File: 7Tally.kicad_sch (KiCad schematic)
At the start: 24 parts, among them J2 B2B-PH-K-S_LF__SN_, P1 53047-0310, SW1 TL3300CF160Q, U1 ESP32-C3_SUPERMINI_TH, U2 BQ21040DBVR, U3 TC1263-3.3VOA

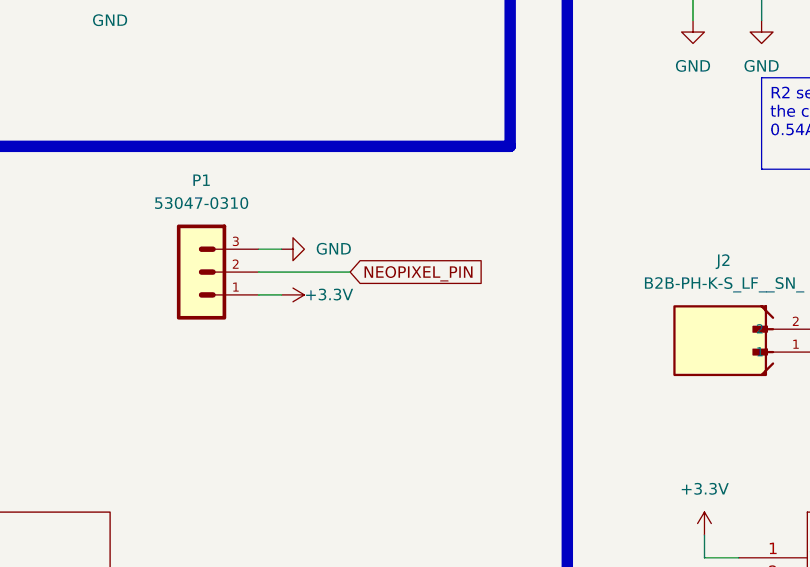
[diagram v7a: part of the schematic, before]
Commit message: feat(PCB): finalized initial PCB
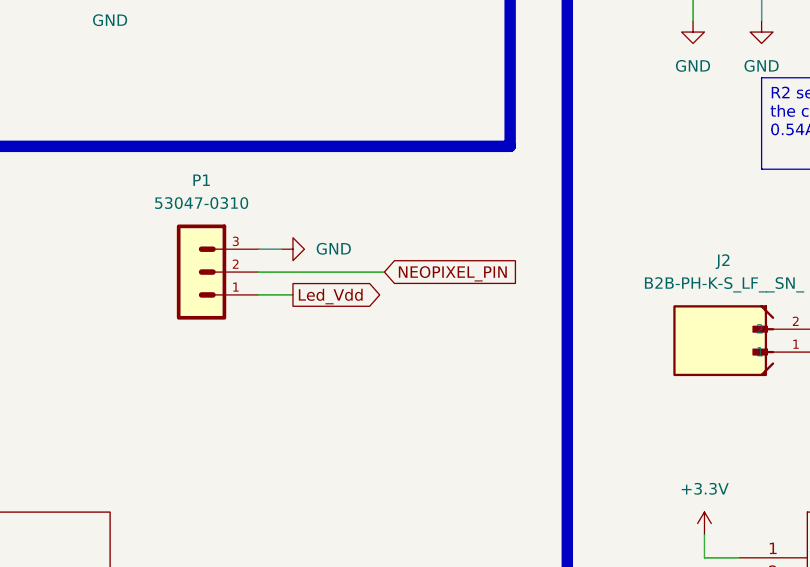
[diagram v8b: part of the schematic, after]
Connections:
- net +3.3V: no longer P1.1
- net Led_Vdd: now also P1.1
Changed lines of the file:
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@@
 	(wire
 		(pts
-			(xy 93.98 95.25) (xy 104.14 95.25)
+			(xy 93.98 95.25) (xy 107.95 95.25)
 		)
 		(stroke
@@
 	(wire
 		(pts
-			(xy 96.52 97.79) (xy 93.98 97.79)
+			(xy 97.79 97.79) (xy 93.98 97.79)
 		)
 		(stroke
@@
 	(global_label "NEOPIXEL_PIN"
 		(shape input)
-		(at 104.14 95.25 0)
+		(at 107.95 95.25 0)
 		(fields_autoplaced yes)
 		(effects
@@
 		)
 		(property "Intersheetrefs" "${INTERSHEET_REFS}"
-			(at 120.3695 95.25 0)
+			(at 124.1795 95.25 0)
 			(effects
 				(font
@@
 				)
 				(justify right)
+				(hide yes)
+			)
+		)
+	)
+	(global_label "Led_Vdd"
+		(shape output)
+		(at 97.79 97.79 0)
+		(fields_autoplaced yes)
+		(effects
+			(font
+				(size 1.27 1.27)
+			)
+			(justify left)
+		)
+		(property "Intersheetrefs" "${INTERSHEET_REFS}"
+			(at 108.3951 97.79 0)
+			(effects
+				(font
+					(size 1.27 1.27)
+				)
+				(justify left)
 				(hide yes)
 			)
@@
 					(unit 1)
 				)
-			)
-		)
-	)
-	(symbol
-		(lib_id "power:+3.3V")
-		(at 96.52 97.79 270)
-		(unit 1)
-		(exclude_from_sim no)
-		(in_bom yes)
-		(on_board yes)
-		(dnp no)
-		(property "Reference" "#PWR022"
-			(at 92.71 97.79 0)
-			(effects
-				(font
-					(size 1.27 1.27)
-				)
-				(hide yes)
-			)
-		)
-		(property "Value" "+3.3V"
-			(at 99.06 97.79 90)
-			(effects
-				(font
-					(size 1.27 1.27)
-				)
-				(justify left)
-			)
-		)
-		(property "Footprint" ""
-			(at 96.52 97.79 0)
-			(effects
-				(font
-					(size 1.27 1.27)
-				)
-				(hide yes)
-			)
-		)
-		(property "Datasheet" ""
-			(at 96.52 97.79 0)
-			(effects
-				(font
-					(size 1.27 1.27)
-				)
-				(hide yes)
-			)
-		)
-		(property "Description" "Power symbol creates a global label with name \"+3.3V\""
-			(at 96.52 97.79 0)
-			(effects
-				(font
-					(size 1.27 1.27)
-				)
-				(hide yes)
-			)
-		)
-		(pin "1"
-		)
-		(instances
-			(project "7Tally"
-				(path "/a26cb5f3-8ba9-4d03-a29e-a58d33583019"
-					(reference "#PWR022")
-					(unit 1)
-				)
